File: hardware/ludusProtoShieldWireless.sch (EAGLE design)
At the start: 85 parts, among them Q1 MOSFET-NCHANNELBSS138, Q2 MOSFET-NCHANNELBSS138, U1 XBEE-1XBEE-1_LOCK, U2 ARDUINO, U3 TB6612FNG

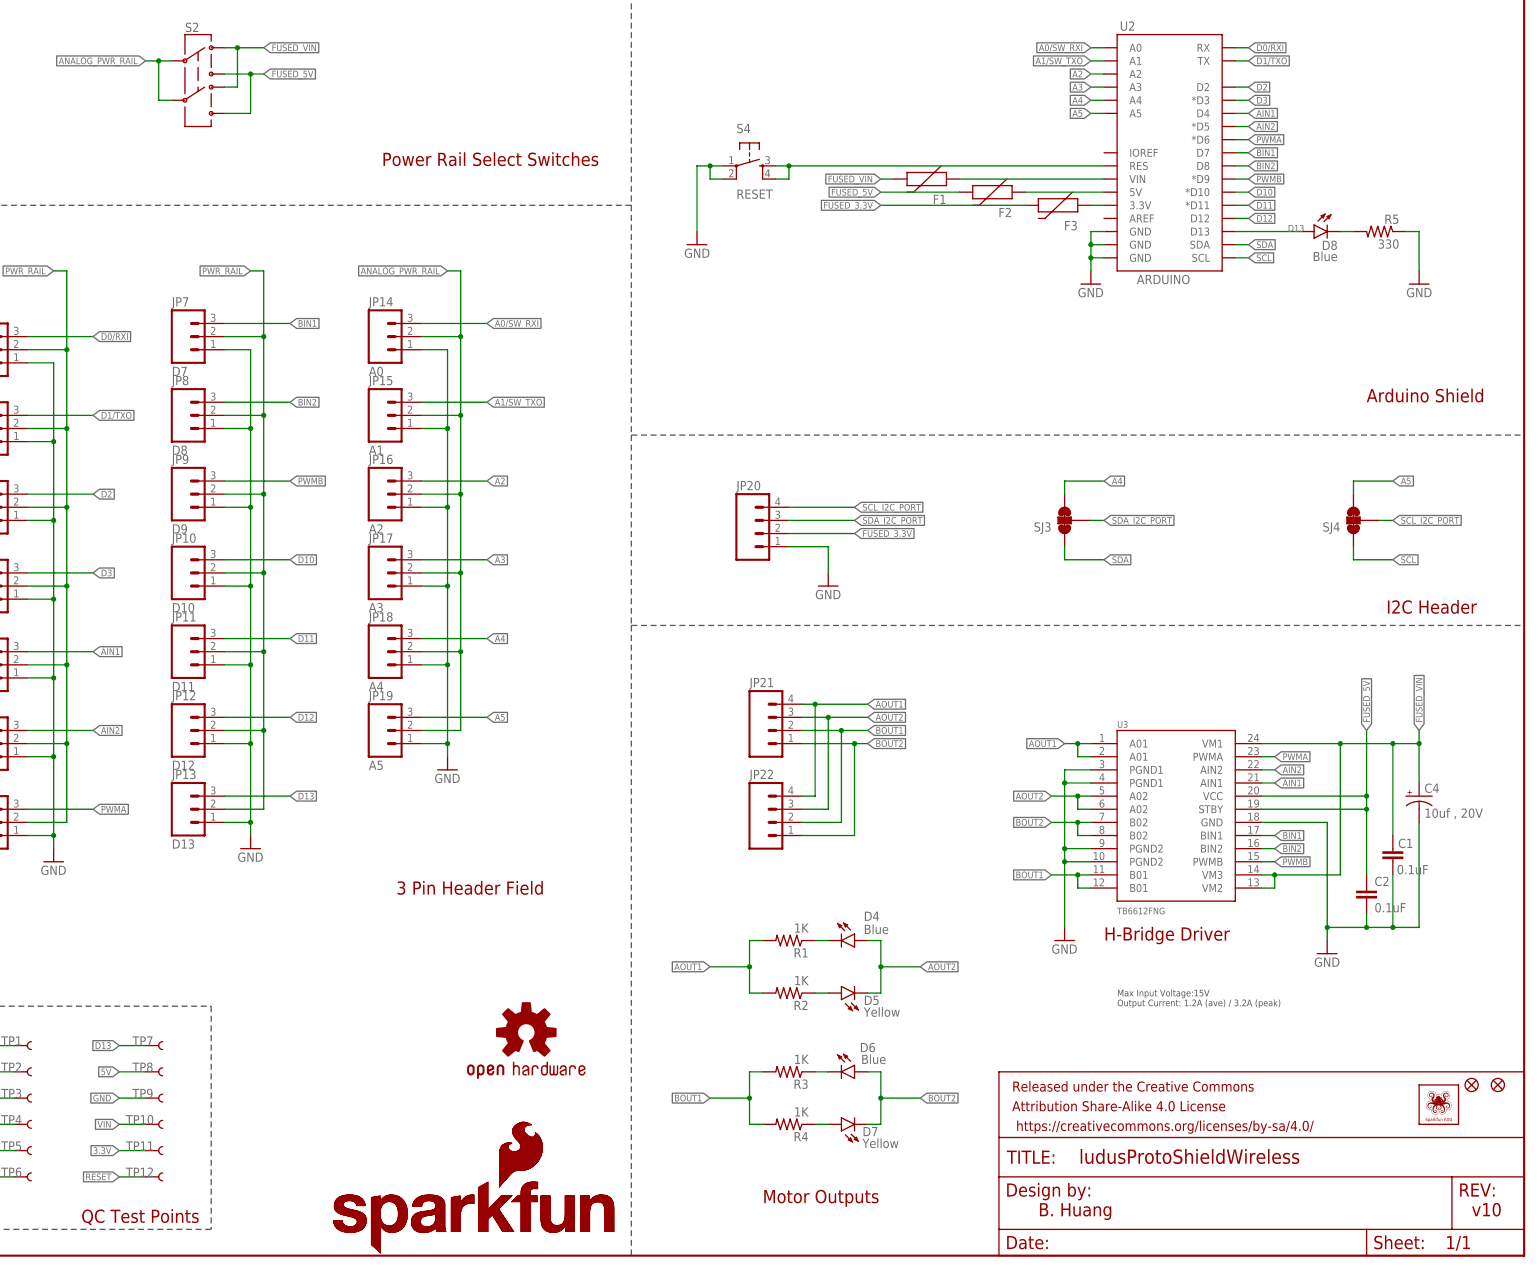
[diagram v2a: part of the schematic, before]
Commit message: Moved PWM pins to 3 and 6 instead of 6 and 9
Changed the PWM control pins on the shield to pins 3 & 6 so that it is
compatible / does not conflict with the Arduino Servo library.

No test points moved. Updated silk accordingly.
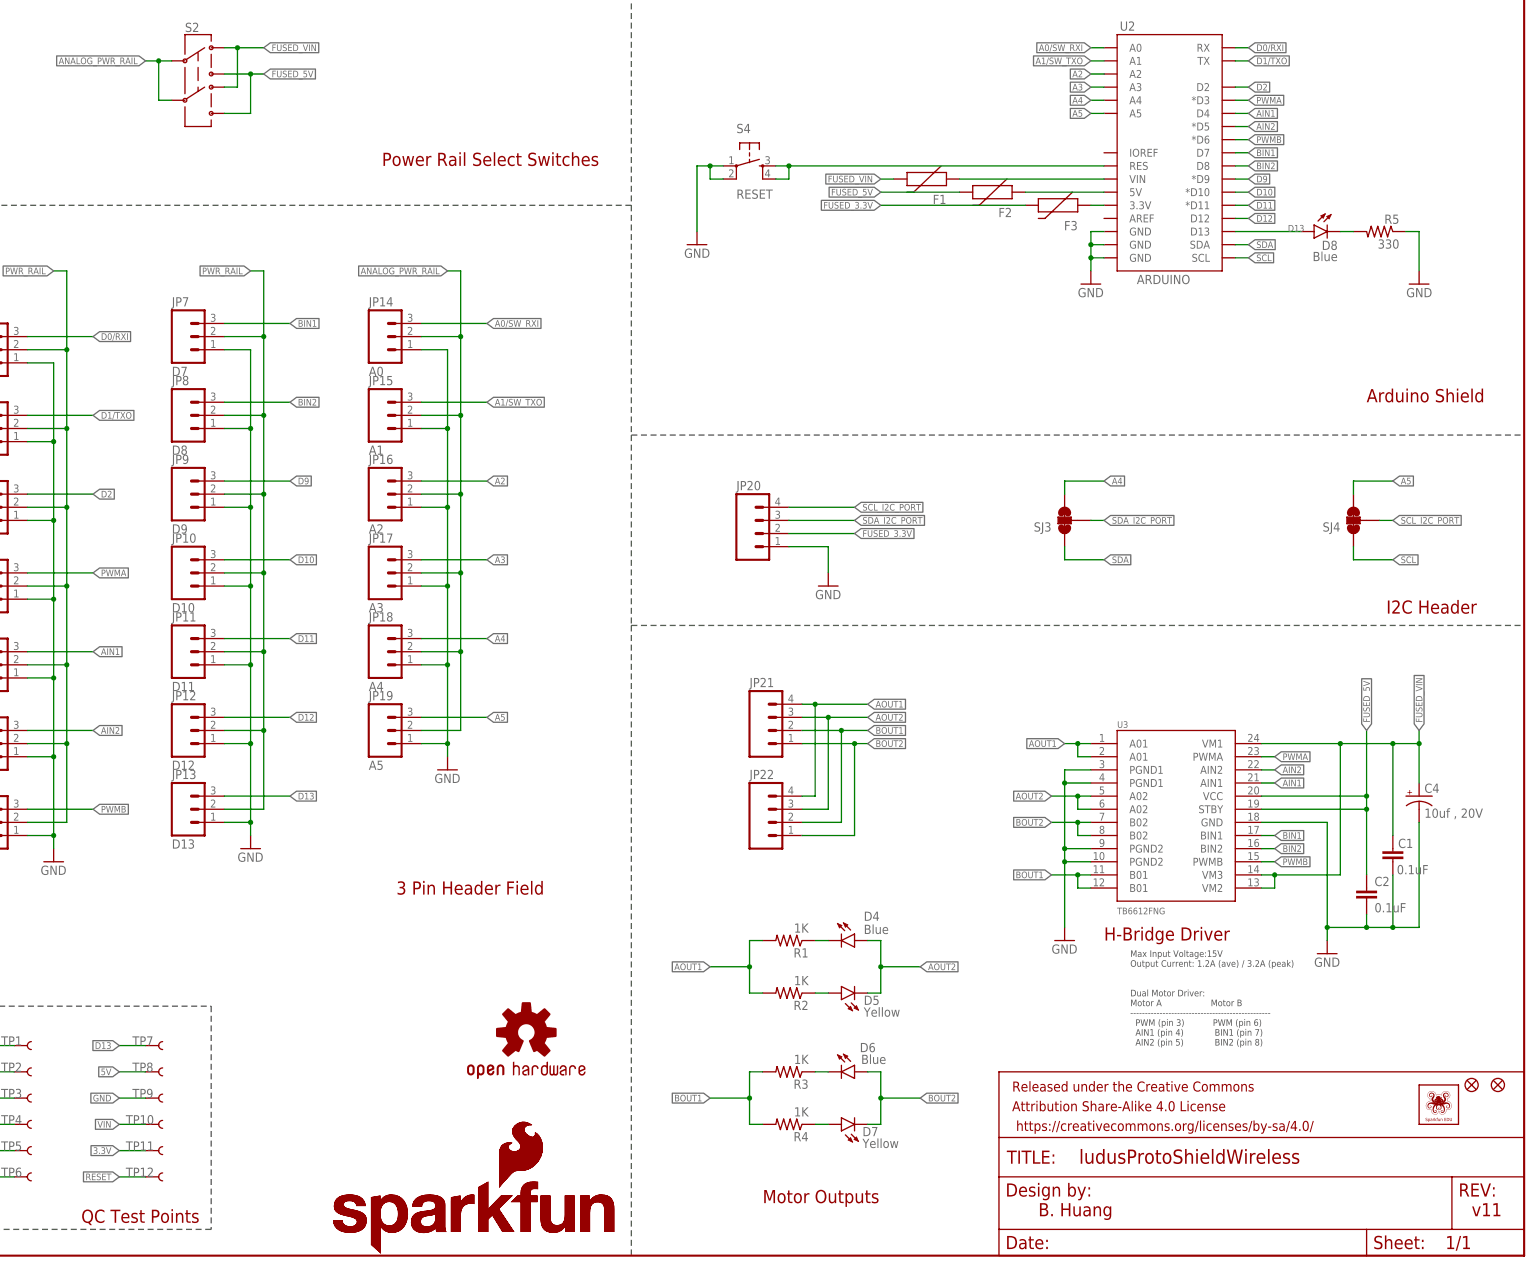
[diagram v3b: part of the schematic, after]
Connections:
- removed net D3: JP3.3, U2.*D3
- new net D9: JP9.3, U2.*D9
- net PWMA: now also JP3.3, U2.*D3; no longer JP6.3, U2.*D6
- net PWMB: now also JP6.3, U2.*D6; no longer JP9.3, U2.*D9
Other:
- note added: "Dual Motor Driver: Motor A Motor B ------------------------------------------------ PWM (pin 3) PWM (pin 6) AIN1 (pin 4) BIN1 (pin 7) AIN2 (pin 5) BIN2 (pin 8)"
- note added: "v11"
- note removed: "v10"
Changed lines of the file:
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@@
 <wire x1="259.08" y1="203.2" x2="259.08" y2="158.75" width="0.2032" layer="97" style="longdash"/>
 <text x="337.82" y="7.62" size="2.54" layer="94">B. Huang</text>
-<text x="421.64" y="7.62" size="2.54" layer="94">v10</text>
+<text x="421.64" y="7.62" size="2.54" layer="94">v11</text>
 <wire x1="259.08" y1="158.75" x2="259.08" y2="121.92" width="0.2032" layer="97" style="longdash"/>
 <wire x1="259.08" y1="121.92" x2="259.08" y2="0" width="0.2032" layer="97" style="longdash"/>
@@
 <wire x1="259.08" y1="158.75" x2="431.8" y2="158.75" width="0.1524" layer="97" style="longdash"/>
 <text x="210.82" y="210.82" size="2.54" layer="94">Power Rail Select Switches</text>
-<text x="353.06" y="48.26" size="1.27" layer="97">Max Input Voltage:15V
+<text x="355.6" y="55.88" size="1.27" layer="97">Max Input Voltage:15V
 Output Current: 1.2A (ave) / 3.2A (peak)</text>
 <text x="12.7" y="142.24" size="1.27" layer="97">RESET Jumper provides easy access
@@
 <wire x1="121.92" y1="5.08" x2="121.92" y2="48.26" width="0.2032" layer="97" style="longdash"/>
 <text x="152.654" y="6.35" size="2.54" layer="94">QC Test Points</text>
+<text x="355.6" y="40.64" size="1.27" layer="97">Dual Motor Driver:
+Motor A                   Motor B
+------------------------------------------------
+  PWM (pin 3)           PWM (pin 6)
+  AIN1 (pin 4)            BIN1 (pin 7)
+  AIN2 (pin 5)            BIN2 (pin 8)</text>
 </plain>
 <instances>
@@
 </segment>
 <segment>
+<pinref part="TP3" gate="G$1" pin="1"/>
+<wire x1="139.7" y1="30.48" x2="134.62" y2="30.48" width="0.1524" layer="91"/>
+<label x="134.62" y="30.48" size="1.27" layer="95" rot="R180" xref="yes"/>
+</segment>
+<segment>
+<wire x1="375.92" y1="223.52" x2="378.46" y2="223.52" width="0.1524" layer="91"/>
+<label x="378.46" y="223.52" size="1.27" layer="95" xref="yes"/>
+<pinref part="U2" gate="G$1" pin="*D3"/>
+</segment>
+<segment>
+<pinref part="JP3" gate="G$1" pin="3"/>
+<wire x1="142.24" y1="132.08" x2="154.94" y2="132.08" width="0.1524" layer="91"/>
+<label x="154.94" y="132.08" size="1.27" layer="95" xref="yes"/>
+</segment>
+</net>
+<net name="PWMB" class="0">
+<segment>
+<pinref part="U3" gate="G$1" pin="PWMB"/>
+<wire x1="381" y1="76.2" x2="383.54" y2="76.2" width="0.1524" layer="91"/>
+<label x="383.54" y="76.2" size="1.27" layer="95" xref="yes"/>
+</segment>
+<segment>
+<pinref part="TP6" gate="G$1" pin="1"/>
+<wire x1="139.7" y1="15.24" x2="134.62" y2="15.24" width="0.1524" layer="91"/>
+<label x="134.62" y="15.24" size="1.27" layer="95" rot="R180" xref="yes"/>
+</segment>
+<segment>
 <pinref part="U2" gate="G$1" pin="*D6"/>
 <wire x1="375.92" y1="215.9" x2="378.46" y2="215.9" width="0.1524" layer="91"/>
@@
 <wire x1="142.24" y1="86.36" x2="154.94" y2="86.36" width="0.1524" layer="91"/>
 <label x="154.94" y="86.36" size="1.27" layer="95" xref="yes"/>
-</segment>
-<segment>
-<pinref part="TP3" gate="G$1" pin="1"/>
-<wire x1="139.7" y1="30.48" x2="134.62" y2="30.48" width="0.1524" layer="91"/>
-<label x="134.62" y="30.48" size="1.27" layer="95" rot="R180" xref="yes"/>
-</segment>
-</net>
-<net name="PWMB" class="0">
-<segment>
-<pinref part="U3" gate="G$1" pin="PWMB"/>
-<wire x1="381" y1="76.2" x2="383.54" y2="76.2" width="0.1524" layer="91"/>
-<label x="383.54" y="76.2" size="1.27" layer="95" xref="yes"/>
-</segment>
-<segment>
-<pinref part="U2" gate="G$1" pin="*D9"/>
-<wire x1="375.92" y1="208.28" x2="378.46" y2="208.28" width="0.1524" layer="91"/>
-<label x="378.46" y="208.28" size="1.27" layer="95" xref="yes"/>
-</segment>
-<segment>
-<pinref part="JP9" gate="G$1" pin="3"/>
-<wire x1="180.34" y1="149.86" x2="193.04" y2="149.86" width="0.1524" layer="91"/>
-<label x="193.04" y="149.86" size="1.27" layer="95" xref="yes"/>
-</segment>
-<segment>
-<pinref part="TP6" gate="G$1" pin="1"/>
-<wire x1="139.7" y1="15.24" x2="134.62" y2="15.24" width="0.1524" layer="91"/>
-<label x="134.62" y="15.24" size="1.27" layer="95" rot="R180" xref="yes"/>
 </segment>
 </net>
@@
 <wire x1="165.1" y1="15.24" x2="160.02" y2="15.24" width="0.1524" layer="91"/>
 <label x="160.02" y="15.24" size="1.27" layer="95" rot="R180" xref="yes"/>
-</segment>
-</net>
-<net name="D3" class="0">
-<segment>
-<wire x1="375.92" y1="223.52" x2="378.46" y2="223.52" width="0.1524" layer="91"/>
-<label x="378.46" y="223.52" size="1.27" layer="95" xref="yes"/>
-<pinref part="U2" gate="G$1" pin="*D3"/>
-</segment>
-<segment>
-<pinref part="JP3" gate="G$1" pin="3"/>
-<wire x1="142.24" y1="132.08" x2="154.94" y2="132.08" width="0.1524" layer="91"/>
-<label x="154.94" y="132.08" size="1.27" layer="95" xref="yes"/>
 </segment>
 </net>
@@
 </segment>
 </net>
+<net name="D9" class="0">
+<segment>
+<pinref part="U2" gate="G$1" pin="*D9"/>
+<wire x1="375.92" y1="208.28" x2="378.46" y2="208.28" width="0.1524" layer="91"/>
+<label x="378.46" y="208.28" size="1.27" layer="95" xref="yes"/>
+</segment>
+<segment>
+<pinref part="JP9" gate="G$1" pin="3"/>
+<wire x1="180.34" y1="149.86" x2="193.04" y2="149.86" width="0.1524" layer="91"/>
+<label x="193.04" y="149.86" size="1.27" layer="95" xref="yes"/>
+</segment>
+</net>

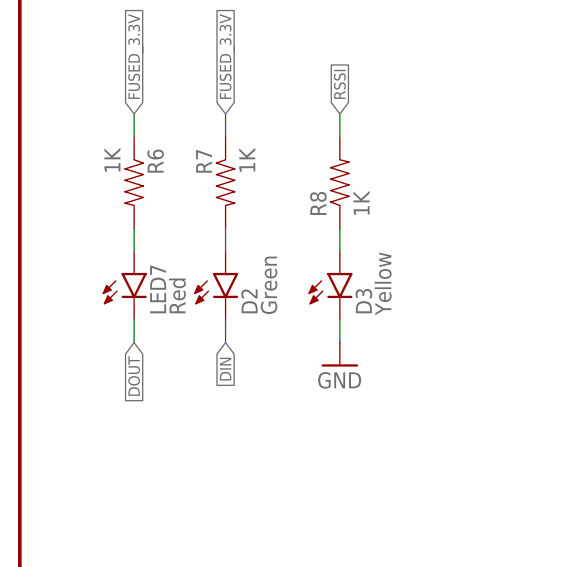
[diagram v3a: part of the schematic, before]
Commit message: Updates re: Issue #4
Fixed labels on LED7 to D1.
Bumped the HW /SW Serial switch over to avoid the silk
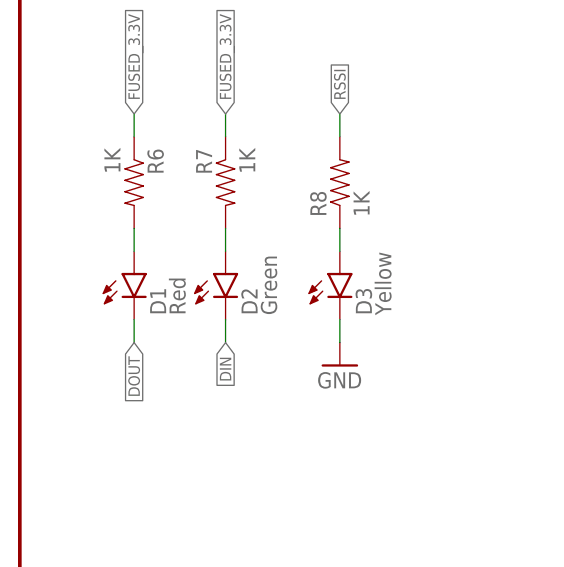
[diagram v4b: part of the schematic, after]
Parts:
- renumbered LED7 to D1
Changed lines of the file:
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@@
 <part name="LOGO4" library="SparkFun-Aesthetics" deviceset="SFE_LOGO_NAME_FLAME" device=".1_INCH" value="SFE_LOGO_NAME_FLAME.1_INCH"/>
 <part name="JP22" library="SparkFun-Connectors" deviceset="M04" device="LOCK"/>
-<part name="LED7" library="SparkFun-LED" deviceset="LED-RED" device="0603" value="Red"/>
+<part name="D1" library="SparkFun-LED" deviceset="LED-RED" device="0603" value="Red"/>
 <part name="D2" library="SparkFun-LED" deviceset="LED-GREEN" device="0603" value="Green"/>
 <part name="R6" library="SparkFun-Resistors" deviceset="1KOHM-1/10W-1%(0603)" device="" value="1K"/>
@@
 <instance part="LOGO4" gate="G$1" x="200.66" y="0"/>
 <instance part="JP22" gate="G$1" x="287.02" y="83.82"/>
-<instance part="LED7" gate="G$1" x="12.7" y="43.18"/>
+<instance part="D1" gate="G$1" x="12.7" y="43.18"/>
 <instance part="D2" gate="G$1" x="22.86" y="43.18"/>
 <instance part="R6" gate="G$1" x="12.7" y="53.34" rot="R270"/>
@@
 <segment>
 <wire x1="12.7" y1="48.26" x2="12.7" y2="45.72" width="0.1524" layer="91"/>
-<pinref part="LED7" gate="G$1" pin="A"/>
+<pinref part="D1" gate="G$1" pin="A"/>
 <pinref part="R6" gate="G$1" pin="2"/>
 </segment>
@@
 <wire x1="12.7" y1="38.1" x2="12.7" y2="35.56" width="0.1524" layer="91"/>
 <label x="12.7" y="35.56" size="1.27" layer="95" rot="R270" xref="yes"/>
-<pinref part="LED7" gate="G$1" pin="C"/>
-</segment>
-</net>
+<pinref part="D1" gate="G$1" pin="C"/>
+</segment>
+</net>
